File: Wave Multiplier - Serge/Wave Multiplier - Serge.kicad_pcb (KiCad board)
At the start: 2 copper layers, 110.2 x 116.8 mm, 152 parts, among them J1 In_T, J10 SW_T_R_2, J11 CV_M, J12 IN_M_1, J13 IN_M_1, J14 VC_M, J15 M_Out, J16 CV_B, J17 In_B_1, J18 In_B_2, J19 VC_B, J2 CV, J20 Out_B_1, J21 Out_B_2, J3 +12V_Conn, J4 GND_Conn, J5 -12V_Conn, J6 VC_T, J7 SW_T_M, J8 SW_T_M_2, J9 Out_T, Q1 BC557, Q2 BC557, U1 LM3900, U2 LM3900, U3 CA3080, U4 TL082, U5 CA3080, U6 TL084, U7 TL084

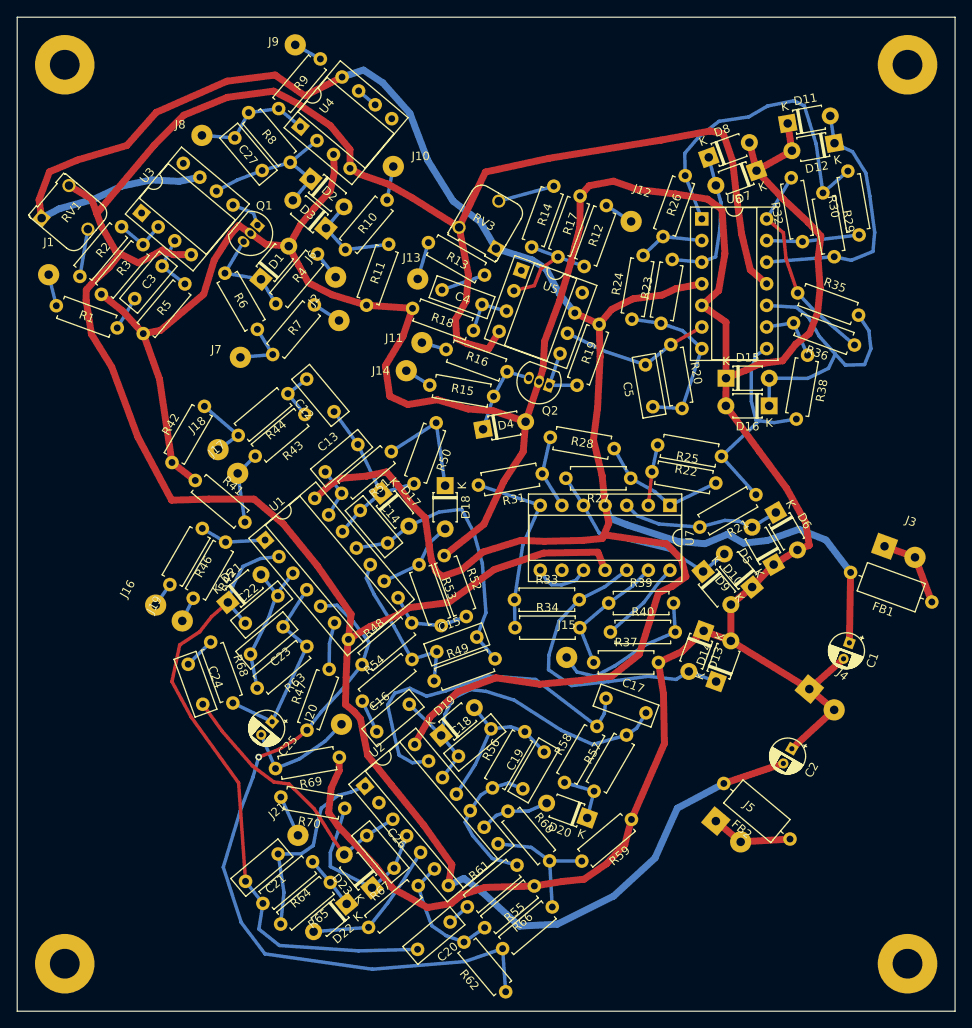
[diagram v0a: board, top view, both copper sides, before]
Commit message: cleaned up silkscreen
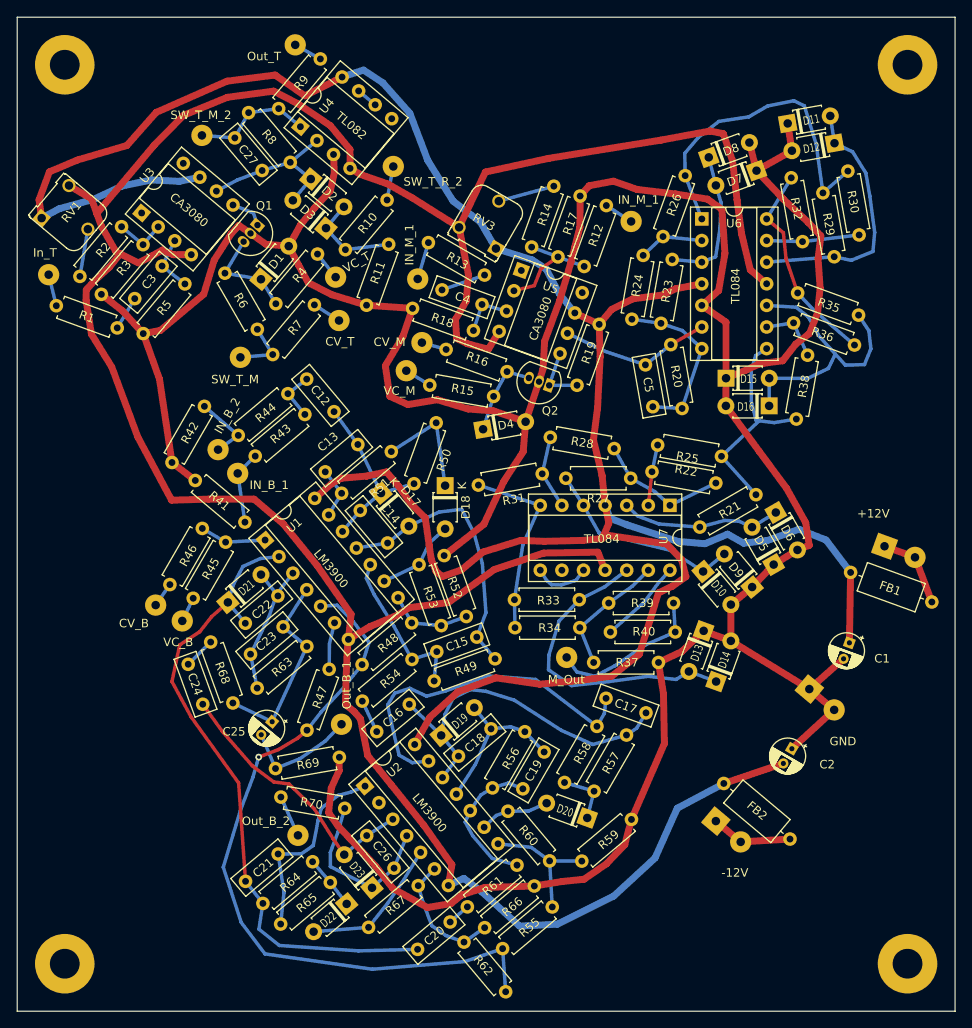
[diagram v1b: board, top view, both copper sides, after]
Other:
- board text added: "+12V"
- board text added: "-12V"
- board text added: "CA3080"
- board text added: "CV_B"
- board text added: "CV_M"
- board text added: "CV_T"
- board text added: "GND"
- board text added: "IN_B_1"
- board text added: "IN_B_2"
- board text added: "IN_M_1"
- board text added: "In_T"
- board text added: "LM3900"
- board text added: "M_Out"
- board text added: "Out_B_1"
- board text added: "Out_B_2"
- board text added: "Out_T"
- board text added: "SW_T_M"
- board text added: "SW_T_M_2"
- board text added: "SW_T_R_2"
- board text added: "TL082"
- board text added: "TL084"
- board text added: "VC_B"
- board text added: "VC_M"
- board text added: "VC_T"

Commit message: literally so much stuff
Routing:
- added copper zone on B.Cu, net Earth
- added copper zone on F.Cu, net Earth
